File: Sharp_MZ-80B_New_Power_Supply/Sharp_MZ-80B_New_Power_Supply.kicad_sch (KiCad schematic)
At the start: 16 parts, among them J1 To Motherboard, J2 DC In, J3 To Tape Deck, J4 To Monitor, U1 PSU5, U2 R-78CK5.0-0.5

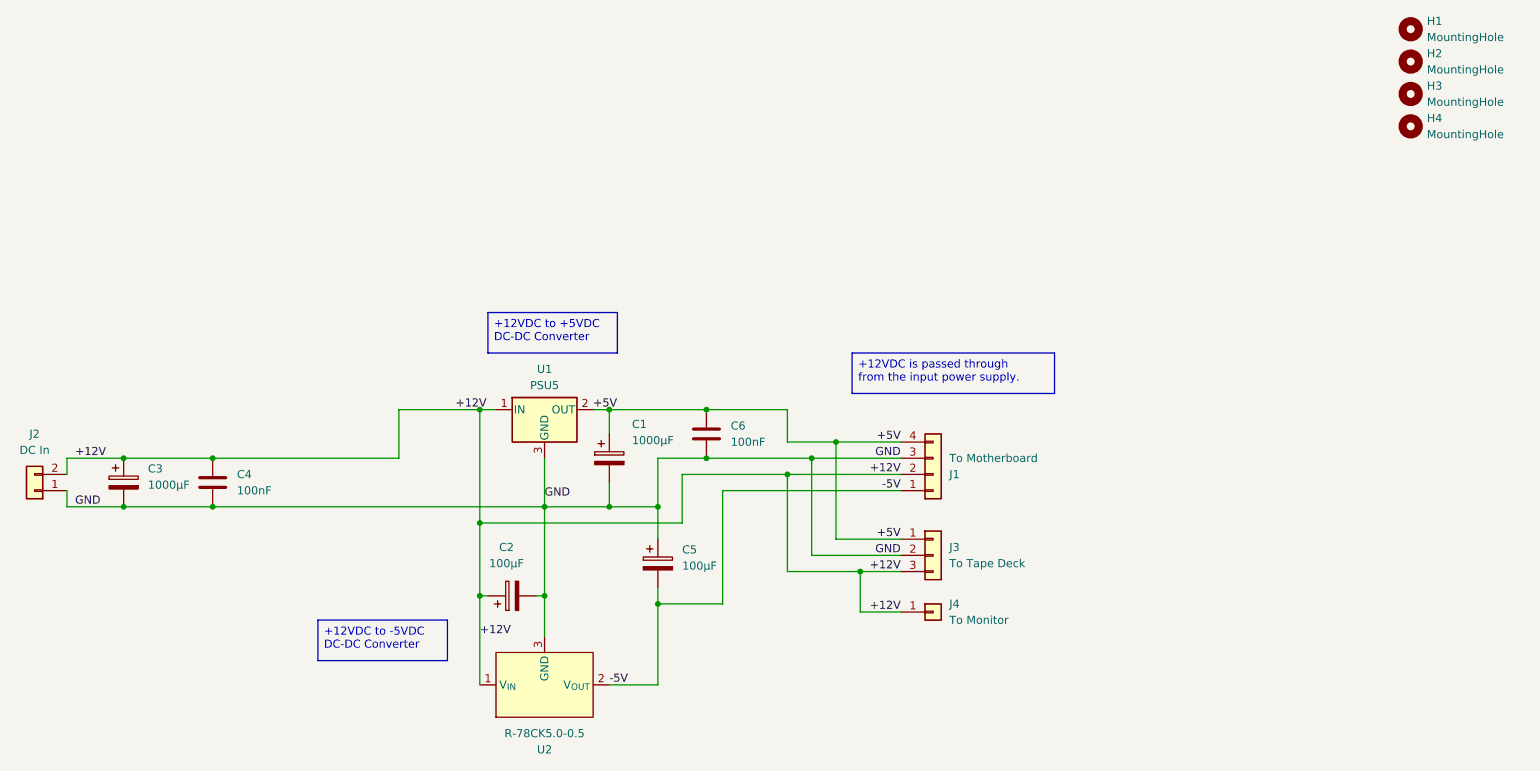
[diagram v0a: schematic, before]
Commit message: Update design to use +15VDC in
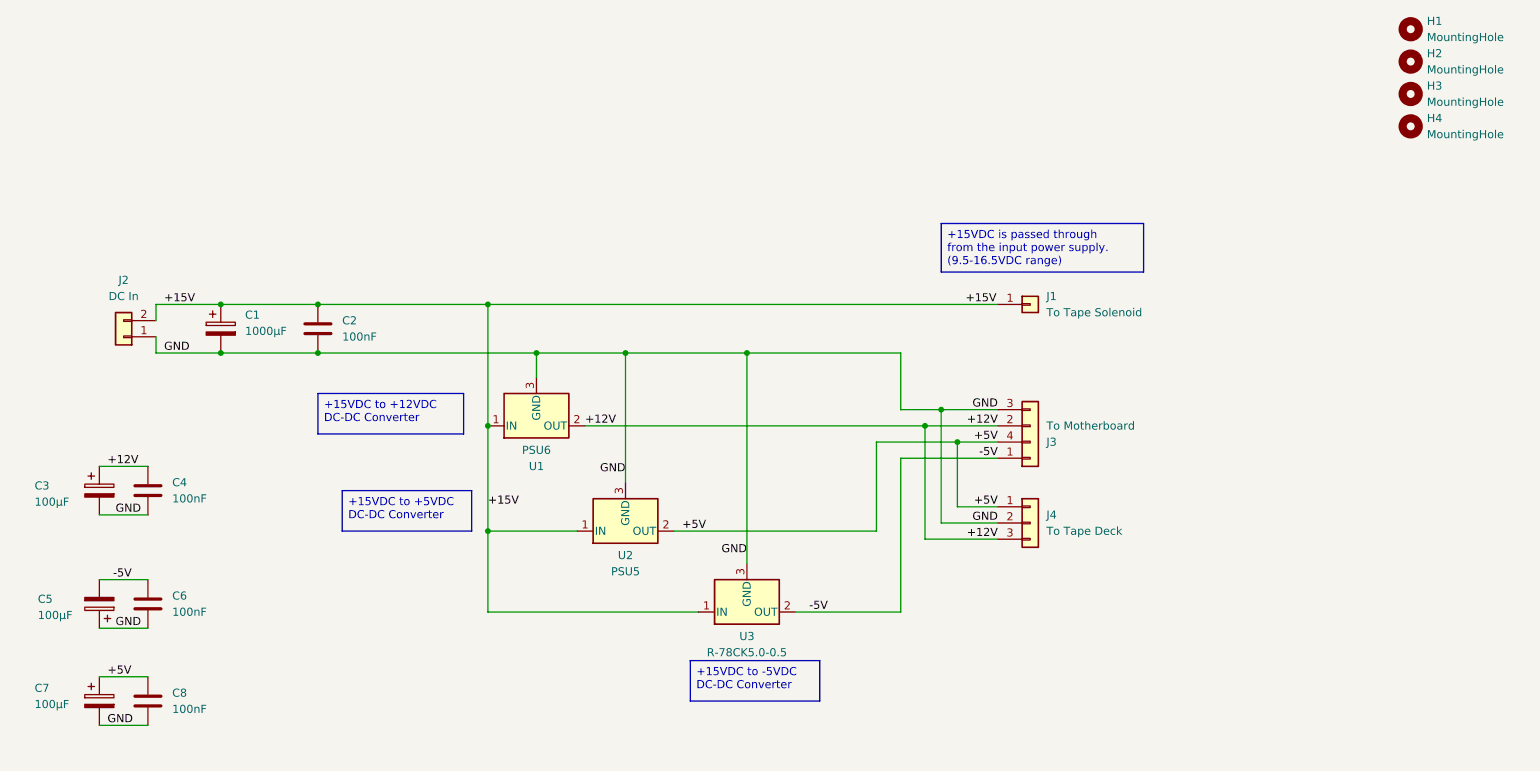
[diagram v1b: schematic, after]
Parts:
- removed C2: 100µF, Capacitor_THT:CP_Radial_D7.5mm_P2.50mm, symbol Device:C_Polarized
- removed U2: R-78CK5.0-0.5, Package_TO_SOT_THT:TO-220-3_Vertical, symbol Clueless_Engineer:R-78CK5.0-0.5
- added C6, C8: 100nF, Capacitor_THT:C_Disc_D3.8mm_W2.6mm_P2.50mm, symbol Device:C
- added C7: 100µF, Capacitor_THT:CP_Radial_D7.5mm_P2.50mm, symbol Device:C_Polarized
- added U1: PSU6, Package_TO_SOT_THT:TO-3, symbol Regulator_Linear:L7805
- added U3: R-78CK5.0-0.5, Package_TO_SOT_THT:TO-220-3_Vertical, symbol Regulator_Linear:L7805
- C3: renamed from C1; value 1000µF -> 100µF; footprint Capacitor_THT:CP_Radial_D16.0mm_P7.50mm -> Capacitor_THT:CP_Radial_D7.5mm_P2.50mm
- J1: renamed from J4; value To Monitor -> To Tape Solenoid
- renumbered C3 to C1, C4 to C2, C6 to C4, J1 to J3, J3 to J4, U1 to U2
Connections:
- net +12V: now also C3.1, C4.1, U1.2 (OUT); no longer C1.1, C2.1, J1.1 (Pin_1), J2.2 (Pin_2), U2.1 (IN)
- net +5V: now also C7.1, C8.1; no longer C3.1, C4.1
- net -5V: now also C6.1, U3.2 (OUT)
- net GND: now also C6.2, C7.2, C8.2, U1.3 (GND), U3.3 (GND)
- new net +15V: C1.1, C2.1, J1.1 (Pin_1), J2.2 (Pin_2), U1.1 (IN), U2.1 (IN), U3.1 (IN)
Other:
- moved on the sheet: C1, C2, C3, C4, J1, J2, J3, J4, U2
